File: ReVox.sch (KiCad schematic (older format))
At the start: 43 parts, among them CN1 EXPANSION_PORT, CN2 AUDIO_OUT, CN3 AUDIO_OUT, J1 CONN_SIGNALS, U1 GAL20V8, U2 74LS273, U3 LM386

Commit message: Refinements
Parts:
- C1, C2, C4, C7: MouserPN (none) -> 810-FG28X7R1H104KNT0
- C10: MouserPN (none) -> 710-860010472002
- C3, C9: MouserPN (none) -> 710-860020573008
- C8: MouserPN (none) -> 810-FG28C0G1H471JNT6
- CN1, J1, V0, V1: MouserPN (none) -> -
- R1, R10, R12, R14, R16, R2, R4, R6, R8: MouserPN (none) -> 603-MFR-25FTE52-22K
- R11, R13, R15, R3, R5, R7, R9: MouserPN (none) -> 603-MFR-25FTE52-11K
- R17: MouserPN (none) -> 603-MFR-25FTF52-10K
- RV1, RV2, RV3: MouserPN (none) -> 652-3306P-1-103
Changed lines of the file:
@@
 F 2 "ReVox:logo" H 11000 11025 50  0001 C CNN
 F 3 "" H 11000 11025 50  0001 C CNN
+F 4 "-" H 11000 11025 50  0001 C CNN "MouserPN"
 	1    11000 11025
 	1    0    0    -1
@@
 F 2 "ReVox:cc_by_nc_sa" H 11000 10800 50  0001 C CNN
 F 3 "" H 11000 10800 50  0001 C CNN
+F 4 "-" H 11000 10800 50  0001 C CNN "MouserPN"
 	1    11000 10800
 	1    0    0    -1
@@
 F 2 "Resistor_THT:R_Axial_DIN0207_L6.3mm_D2.5mm_P10.16mm_Horizontal" V 1685 6215 50  0001 C CNN
 F 3 "~" H 1755 6215 50  0001 C CNN
+F 4 "603-MFR-25FTE52-22K" H 1755 6215 50  0001 C CNN "MouserPN"
 	1    1755 6215
 	1    0    0    -1
@@
 F 2 "Resistor_THT:R_Axial_DIN0207_L6.3mm_D2.5mm_P10.16mm_Horizontal" V 2045 6485 50  0001 C CNN
 F 3 "~" H 2115 6485 50  0001 C CNN
+F 4 "603-MFR-25FTE52-11K" H 2115 6485 50  0001 C CNN "MouserPN"
 	1    2115 6485
 	0    1    1    0
@@
 F 2 "Resistor_THT:R_Axial_DIN0207_L6.3mm_D2.5mm_P10.16mm_Horizontal" V 1685 6740 50  0001 C CNN
 F 3 "~" H 1755 6740 50  0001 C CNN
+F 4 "603-MFR-25FTE52-22K" H 1755 6740 50  0001 C CNN "MouserPN"
 	1    1755 6740
 	1    0    0    -1
@@
 F 2 "Resistor_THT:R_Axial_DIN0207_L6.3mm_D2.5mm_P10.16mm_Horizontal" V 2365 6215 50  0001 C CNN
 F 3 "~" H 2435 6215 50  0001 C CNN
+F 4 "603-MFR-25FTE52-22K" H 2435 6215 50  0001 C CNN "MouserPN"
 	1    2435 6215
 	1    0    0    -1
@@
 F 2 "Resistor_THT:R_Axial_DIN0207_L6.3mm_D2.5mm_P10.16mm_Horizontal" V 2690 6485 50  0001 C CNN
 F 3 "~" H 2760 6485 50  0001 C CNN
+F 4 "603-MFR-25FTE52-11K" H 2760 6485 50  0001 C CNN "MouserPN"
 	1    2760 6485
 	0    1    1    0
@@
 F 2 "Resistor_THT:R_Axial_DIN0207_L6.3mm_D2.5mm_P10.16mm_Horizontal" V 3010 6215 50  0001 C CNN
 F 3 "~" H 3080 6215 50  0001 C CNN
+F 4 "603-MFR-25FTE52-22K" H 3080 6215 50  0001 C CNN "MouserPN"
 	1    3080 6215
 	1    0    0    -1
@@
 F 2 "Resistor_THT:R_Axial_DIN0207_L6.3mm_D2.5mm_P10.16mm_Horizontal" V 3335 6485 50  0001 C CNN
 F 3 "~" H 3405 6485 50  0001 C CNN
+F 4 "603-MFR-25FTE52-11K" H 3405 6485 50  0001 C CNN "MouserPN"
 	1    3405 6485
 	0    1    1    0
@@
 F 2 "Resistor_THT:R_Axial_DIN0207_L6.3mm_D2.5mm_P10.16mm_Horizontal" V 3655 6215 50  0001 C CNN
 F 3 "~" H 3725 6215 50  0001 C CNN
+F 4 "603-MFR-25FTE52-22K" H 3725 6215 50  0001 C CNN "MouserPN"
 	1    3725 6215
 	1    0    0    -1
@@
 F 2 "Resistor_THT:R_Axial_DIN0207_L6.3mm_D2.5mm_P10.16mm_Horizontal" V 3980 6485 50  0001 C CNN
 F 3 "~" H 4050 6485 50  0001 C CNN
+F 4 "603-MFR-25FTE52-11K" H 4050 6485 50  0001 C CNN "MouserPN"
 	1    4050 6485
 	0    1    1    0
@@
 F 2 "Resistor_THT:R_Axial_DIN0207_L6.3mm_D2.5mm_P10.16mm_Horizontal" V 4300 6215 50  0001 C CNN
 F 3 "~" H 4370 6215 50  0001 C CNN
+F 4 "603-MFR-25FTE52-22K" H 4370 6215 50  0001 C CNN "MouserPN"
 	1    4370 6215
 	1    0    0    -1
@@
 F 2 "Resistor_THT:R_Axial_DIN0207_L6.3mm_D2.5mm_P10.16mm_Horizontal" V 4625 6485 50  0001 C CNN
 F 3 "~" H 4695 6485 50  0001 C CNN
+F 4 "603-MFR-25FTE52-11K" H 4695 6485 50  0001 C CNN "MouserPN"
 	1    4695 6485
 	0    1    1    0
@@
 F 2 "Resistor_THT:R_Axial_DIN0207_L6.3mm_D2.5mm_P10.16mm_Horizontal" V 4945 6215 50  0001 C CNN
 F 3 "~" H 5015 6215 50  0001 C CNN
+F 4 "603-MFR-25FTE52-22K" H 5015 6215 50  0001 C CNN "MouserPN"
 	1    5015 6215
 	1    0    0    -1
@@
 F 2 "Resistor_THT:R_Axial_DIN0207_L6.3mm_D2.5mm_P10.16mm_Horizontal" V 5270 6485 50  0001 C CNN
 F 3 "~" H 5340 6485 50  0001 C CNN
+F 4 "603-MFR-25FTE52-11K" H 5340 6485 50  0001 C CNN "MouserPN"
 	1    5340 6485
 	0    1    1    0
@@
 F 2 "Resistor_THT:R_Axial_DIN0207_L6.3mm_D2.5mm_P10.16mm_Horizontal" V 5590 6215 50  0001 C CNN
 F 3 "~" H 5660 6215 50  0001 C CNN
+F 4 "603-MFR-25FTE52-22K" H 5660 6215 50  0001 C CNN "MouserPN"
 	1    5660 6215
 	1    0    0    -1
@@
 F 2 "Resistor_THT:R_Axial_DIN0207_L6.3mm_D2.5mm_P10.16mm_Horizontal" V 5915 6485 50  0001 C CNN
 F 3 "~" H 5985 6485 50  0001 C CNN
+F 4 "603-MFR-25FTE52-11K" H 5985 6485 50  0001 C CNN "MouserPN"
 	1    5985 6485
 	0    1    1    0
@@
 F 2 "Resistor_THT:R_Axial_DIN0207_L6.3mm_D2.5mm_P10.16mm_Horizontal" V 6235 6215 50  0001 C CNN
 F 3 "~" H 6305 6215 50  0001 C CNN
+F 4 "603-MFR-25FTE52-22K" H 6305 6215 50  0001 C CNN "MouserPN"
 	1    6305 6215
 	1    0    0    -1
@@
 F 2 "Capacitor_THT:C_Disc_D7.0mm_W2.5mm_P5.00mm" H 6668 6335 50  0001 C CNN
 F 3 "~" H 6630 6485 50  0001 C CNN
+F 4 "810-FG28X7R1H104KNT0" H 6630 6485 50  0001 C CNN "MouserPN"
 	1    6630 6485
 	0    1    1    0
@@
 F 2 "Capacitor_THT:C_Disc_D7.0mm_W2.5mm_P5.00mm" H 2838 9930 50  0001 C CNN
 F 3 "~" H 2800 10080 50  0001 C CNN
+F 4 "810-FG28X7R1H104KNT0" H 2800 10080 50  0001 C CNN "MouserPN"
 	1    2800 10080
 	1    0    0    -1
@@
 F 2 "Capacitor_THT:C_Disc_D7.0mm_W2.5mm_P5.00mm" H 10703 6555 50  0001 C CNN
 F 3 "~" H 10665 6705 50  0001 C CNN
+F 4 "810-FG28C0G1H471JNT6" H 10665 6705 50  0001 C CNN "MouserPN"
 	1    10665 6705
 	0    -1   -1   0
@@
 F 2 "Resistor_THT:R_Axial_DIN0207_L6.3mm_D2.5mm_P10.16mm_Horizontal" V 11475 5795 50  0001 C CNN
 F 3 "~" H 11545 5795 50  0001 C CNN
+F 4 "603-MFR-25FTF52-10K" H 11545 5795 50  0001 C CNN "MouserPN"
 	1    11545 5795
 	0    1    1    0
@@
 F 2 "Capacitor_THT:CP_Radial_D5.0mm_P2.00mm" H 11845 5990 50  0001 C CNN
 F 3 "~" H 11845 5990 50  0001 C CNN
+F 4 "710-860010472002" H 11845 5990 50  0001 C CNN "MouserPN"
 	1    11845 5990
 	1    0    0    -1
@@
 F 2 "Capacitor_THT:CP_Radial_D6.3mm_P2.50mm" H 2350 10080 50  0001 C CNN
 F 3 "~" H 2350 10080 50  0001 C CNN
+F 4 "710-860020573008" H 2350 10080 50  0001 C CNN "MouserPN"
 	1    2350 10080
 	1    0    0    -1
@@
 F 2 "ReVox:Pot_Bourns_3306P" H 11240 7360 50  0001 C CNN
 F 3 "~" H 11240 7360 50  0001 C CNN
+F 4 "652-3306P-1-103" H 11240 7360 50  0001 C CNN "MouserPN"
 	1    11240 7360
 	0    -1   -1   0
@@
 F 2 "Capacitor_THT:CP_Radial_D6.3mm_P2.50mm" H 10835 7360 50  0001 C CNN
 F 3 "~" H 10835 7360 50  0001 C CNN
+F 4 "710-860020573008" H 10835 7360 50  0001 C CNN "MouserPN"
 	1    10835 7360
 	0    1    1    0
@@
 F 2 "ReVox:Pot_Bourns_3306P" H 11845 7360 50  0001 C CNN
 F 3 "~" H 11845 7360 50  0001 C CNN
+F 4 "652-3306P-1-103" H 11845 7360 50  0001 C CNN "MouserPN"
 	1    11845 7360
 	0    -1   -1   0
@@
 F 2 "Capacitor_THT:C_Disc_D7.0mm_W2.5mm_P5.00mm" H 1643 9930 50  0001 C CNN
 F 3 "~" H 1605 10080 50  0001 C CNN
+F 4 "810-FG28X7R1H104KNT0" H 1605 10080 50  0001 C CNN "MouserPN"
 	1    1605 10080
 	1    0    0    -1
@@
 F 2 "" H 6420 2875 50  0001 C CNN
 F 3 "~" H 6420 2875 50  0001 C CNN
+F 4 "-" H 6420 2875 50  0001 C CNN "MouserPN"
 	1    6420 2875
 	1    0    0    -1
@@
 F 2 "ReVox:C16_Cart_Conn" H 2640 1225 50  0001 C CNN
 F 3 "DOCUMENTATION" H 2640 1125 50  0001 C CNN
+F 4 "-" H 2640 2875 50  0001 C CNN "MouserPN"
 	1    2640 2875
 	1    0    0    -1
@@
 F 2 "Capacitor_THT:C_Disc_D7.0mm_W2.5mm_P5.00mm" H 1118 9925 50  0001 C CNN
 F 3 "~" H 1080 10075 50  0001 C CNN
+F 4 "810-FG28X7R1H104KNT0" H 1080 10075 50  0001 C CNN "MouserPN"
 	1    1080 10075
 	1    0    0    -1
@@
 F 2 "ReVox:Pot_Bourns_3306P" H 9960 6255 50  0001 C CNN
 F 3 "~" H 9960 6255 50  0001 C CNN
+F 4 "652-3306P-1-103" H 9960 6255 50  0001 C CNN "MouserPN"
 	1    9960 6255
 	1    0    0    -1

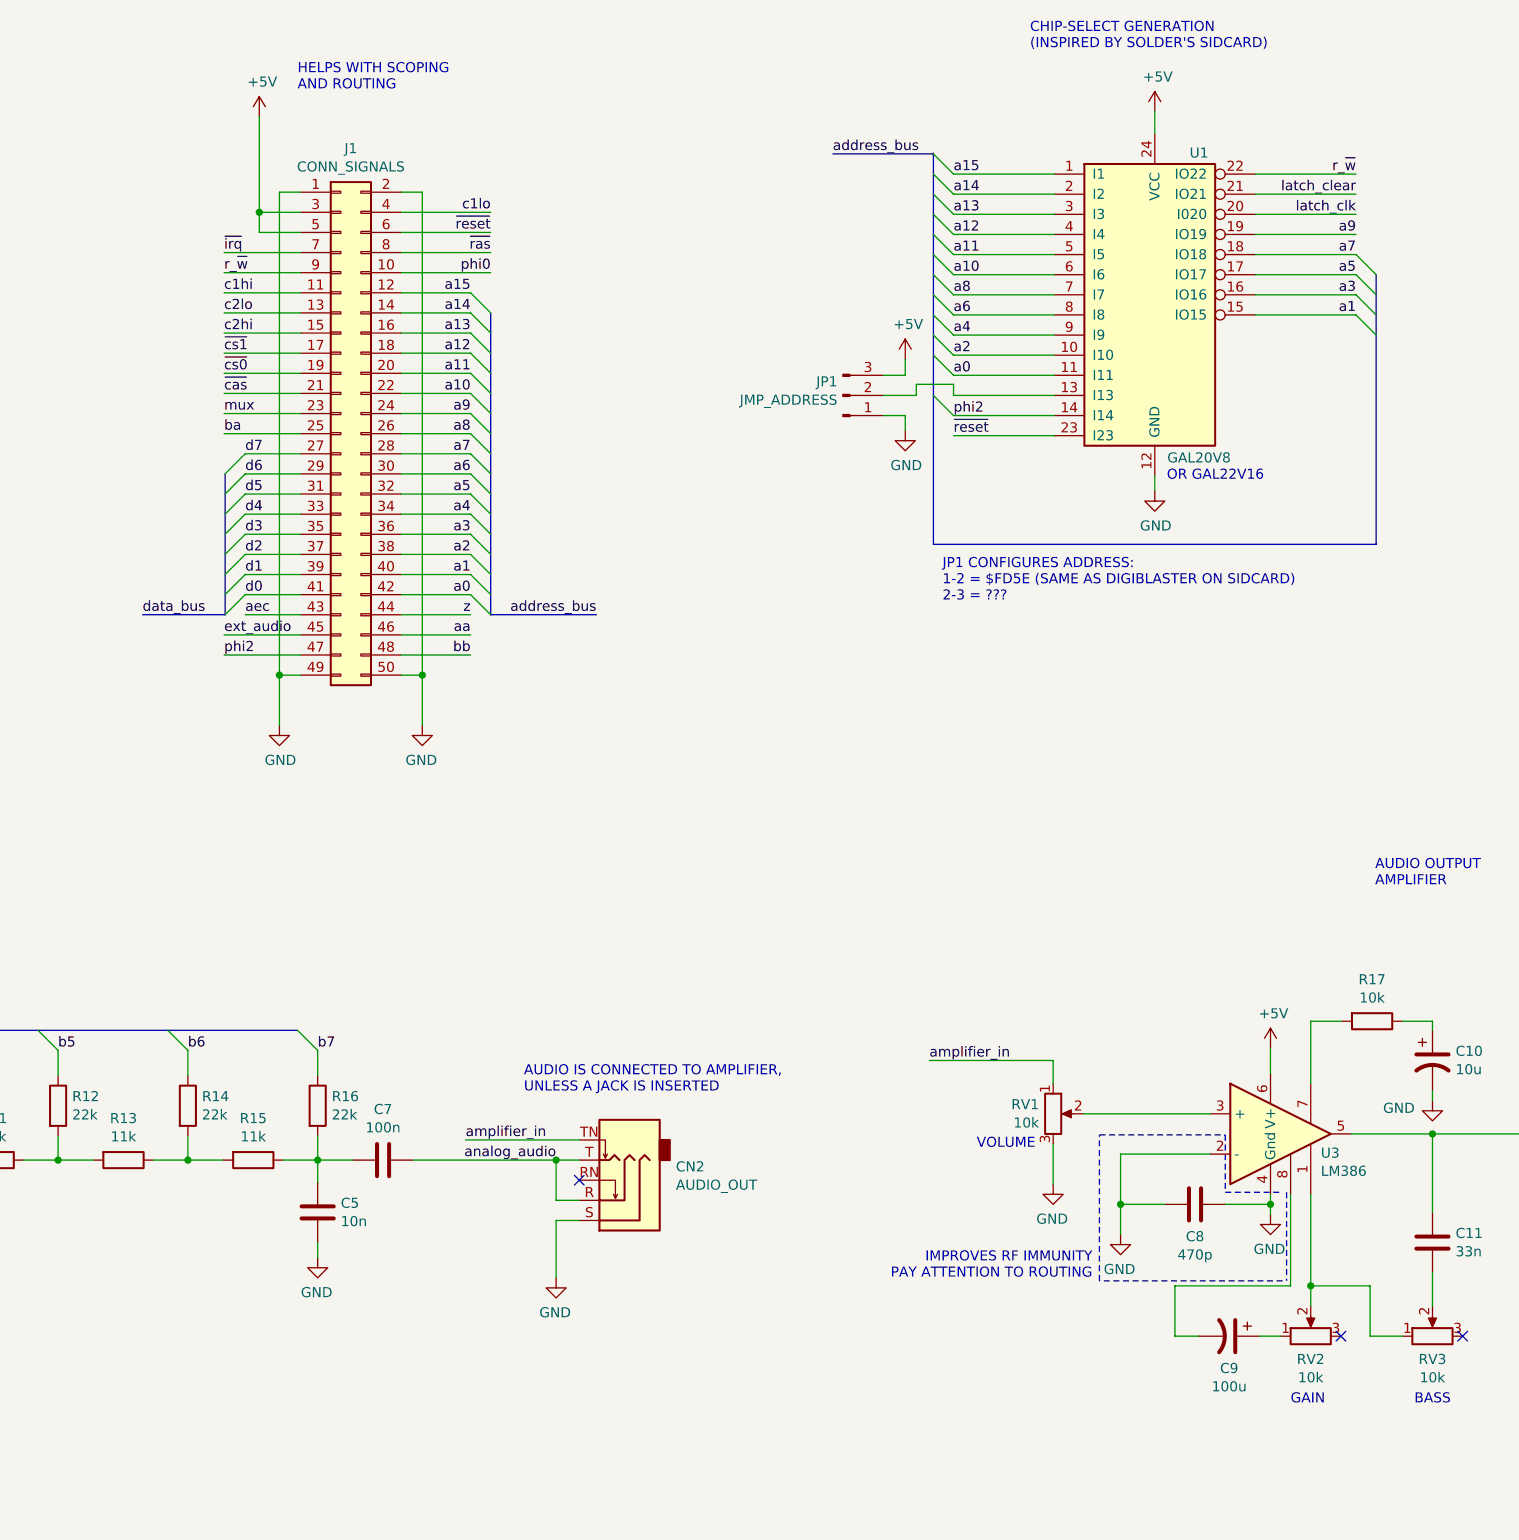
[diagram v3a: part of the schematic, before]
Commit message: Shuffle some things around so that GAL20 is usable too
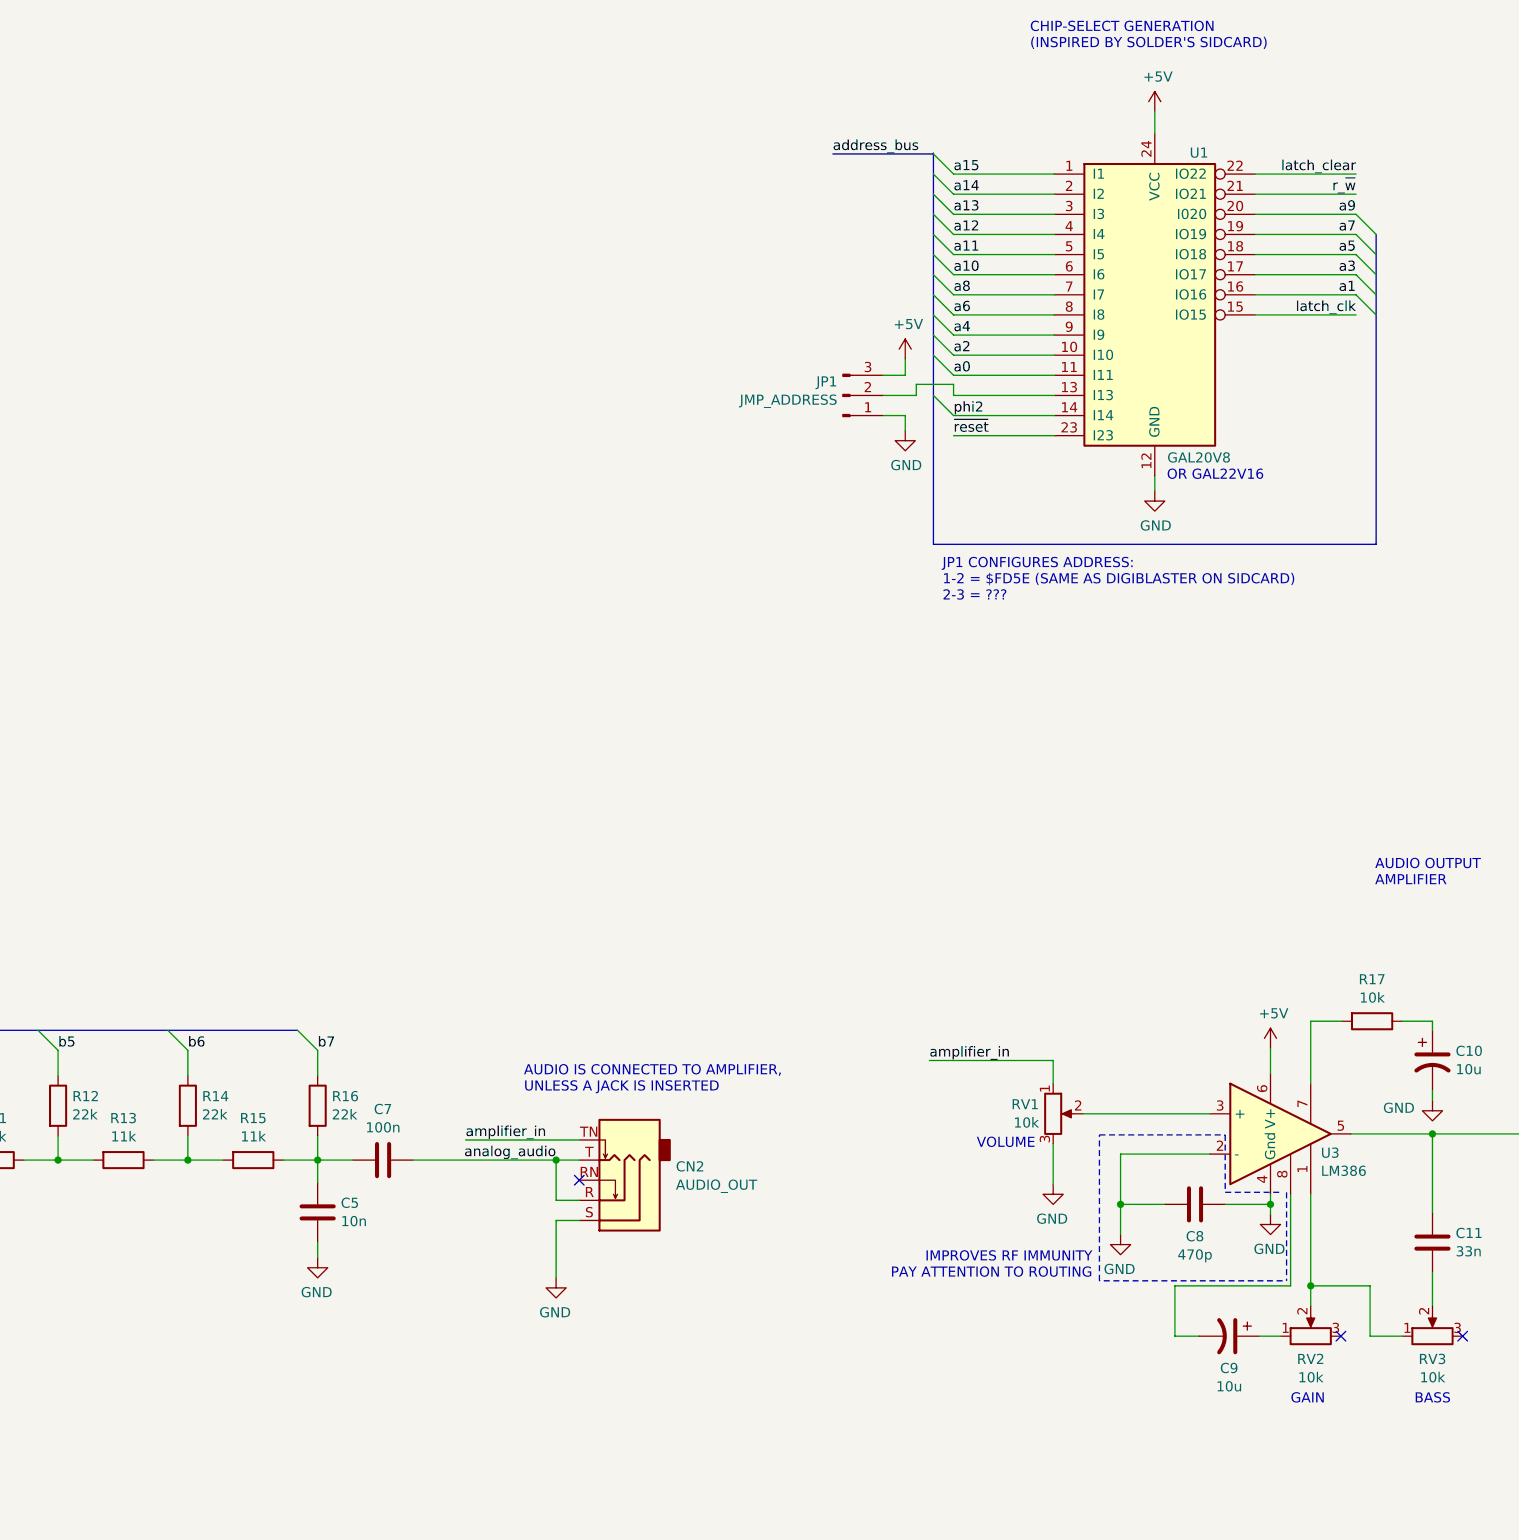
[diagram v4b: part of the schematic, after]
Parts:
- removed J1: CONN_SIGNALS, symbol Connector_Generic:Conn_02x25_Odd_Even
- C9: value 100u -> 10u; footprint Capacitor_THT:CP_Radial_D6.3mm_P2.50mm -> Capacitor_THT:CP_Radial_D5.0mm_P2.00mm
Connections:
- net a1: now also U1.16 (IO16); no longer U1.15 (IO15)
- net a3: now also U1.17 (IO17); no longer U1.16 (IO16)
- net a5: now also U1.18 (IO18); no longer U1.17 (IO17)
- net a7: now also U1.19 (IO19); no longer U1.18 (IO18)
- net a9: now also U1.20 (I020); no longer U1.19 (IO19)
- net latch_clear: now also U1.22 (IO22); no longer U1.21 (IO21)
- net latch_clk: now also U1.15 (IO15); no longer U1.20 (I020)
- net r_~w: now also U1.21 (IO21); no longer U1.22 (IO22)
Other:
- note removed: "HELPS WITH SCOPING\nAND ROUTING"

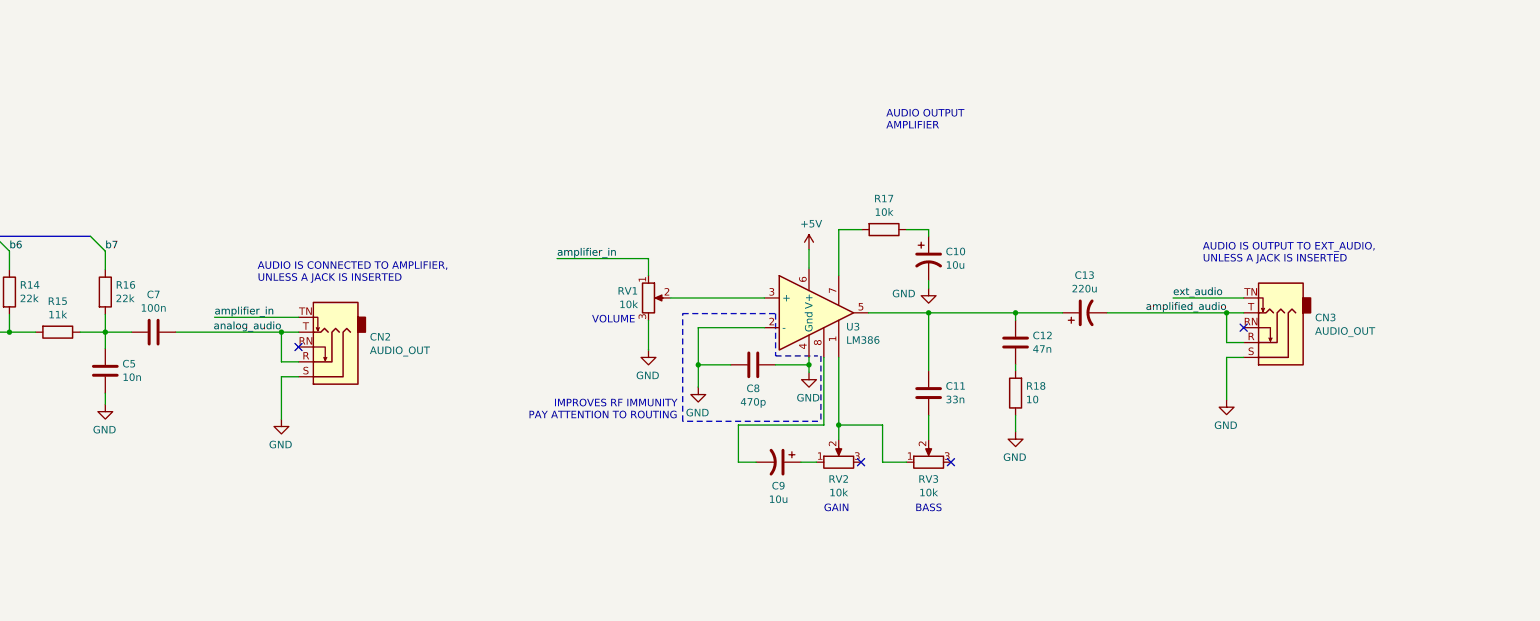
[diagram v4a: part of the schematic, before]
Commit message: Add pin header with raw DAC signal, useful for testing
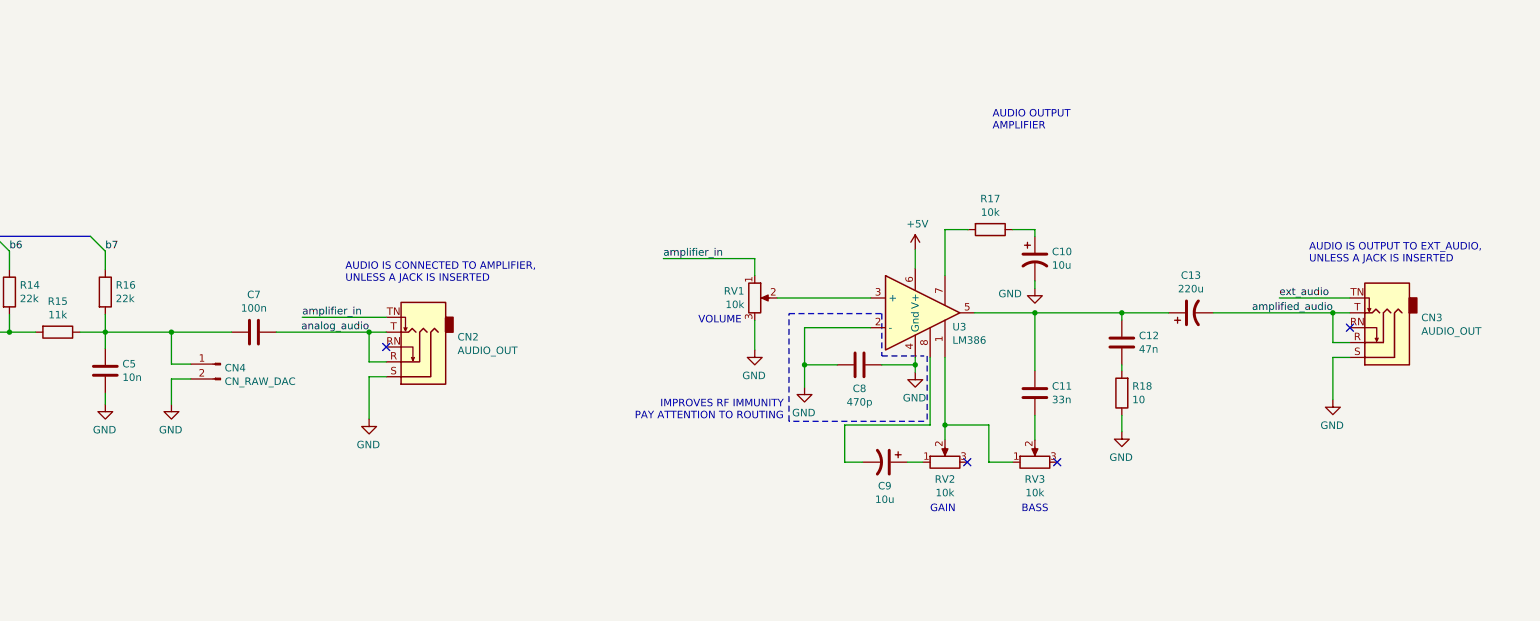
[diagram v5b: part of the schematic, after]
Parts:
- added CN4: CN_RAW_DAC, Connector_PinHeader_2.54mm:PinHeader_1x02_P2.54mm_Vertical, symbol Connector:Conn_01x02_Male
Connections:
- net GND: now also CN4.2 (Pin_2)
- net at C5.2, C7.2, R15.1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: now also CN4.1 (Pin_1)
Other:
- moved on the sheet: C10, C11, C12, C13, C7, C8, C9, CN2, CN3, R17, R18, RV1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
